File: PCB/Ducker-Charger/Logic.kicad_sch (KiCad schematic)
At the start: 47 parts, among them CN1 C_Pack04, IC2 TPS54202HDDCT, J6 Debug, J7 Conn_01x08, J8 Conn_01x07, SW1 EC11E15244G1, U7 STM32F401RBT6, Y1 16MHz

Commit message: fix: minor fixes
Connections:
- net BOOT is gone; now on net BOOT0: U7.60 (BOOT0)
- net SCL is gone; now on net I2C_LP.SCL: J7.4 (Pin_4)
- net SDA is gone; now on net I2C_LP.SDA: J7.3 (Pin_3)
- net ENC_A: no longer C52.1, R50.2, SW1.B, U7.38 (PC7)
- new net ENC_B: C52.1, R50.2, SW1.B, U7.38 (PC7)
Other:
- moved on the sheet: CN1, D21, JP1, R31, R32, R34, R52, R53, R54, RN1, U7

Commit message: feat: updated footprints
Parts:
- C28, C31, C32, C33, C34, C35, C38, C39: footprint (none) -> Capacitor_SMD:C_0805_2012Metric
- C29, C30, C36, C37, C40, C51, C52, C53: footprint (none) -> Capacitor_SMD:C_0603_1608Metric
- CN1: footprint (none) -> Resistor_SMD:R_Array_Concave_4x0603
- CVBAT1, R26, R27, R28, R29, R30, R31, R32, R49, R50, R51, R52, R53: footprint (none) -> Resistor_SMD:R_0603_1608Metric
- FB1: footprint (none) -> Inductor_SMD:L_0603_1608Metric
- L5: footprint (none) -> Inductor_SMD:L_6.3x6.3_H3
- RN1: footprint (none) -> Resistor_SMD:R_Array_Convex_4x0603
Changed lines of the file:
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@@
 			)
 		)
-		(property "Footprint" ""
+		(property "Footprint" "Capacitor_SMD:C_0805_2012Metric"
 			(at 100.0252 35.56 0)
 			(effects
@@
 			)
 		)
-		(property "Footprint" ""
+		(property "Footprint" "Capacitor_SMD:C_0805_2012Metric"
 			(at 88.5952 35.56 0)
 			(effects
@@
 			)
 		)
-		(property "Footprint" ""
+		(property "Footprint" "Capacitor_SMD:C_0603_1608Metric"
 			(at 45.4152 34.29 0)
 			(effects
@@
 			)
 		)
-		(property "Footprint" ""
+		(property "Footprint" "Capacitor_SMD:C_0603_1608Metric"
 			(at 60.6552 160.02 0)
 			(effects
@@
 			)
 		)
-		(property "Footprint" ""
+		(property "Footprint" "Resistor_SMD:R_0603_1608Metric"
 			(at 176.022 82.55 90)
 			(effects
@@
 			)
 		)
-		(property "Footprint" ""
+		(property "Footprint" "Resistor_SMD:R_0603_1608Metric"
 			(at 176.022 127 90)
 			(effects
@@
 			)
 		)
-		(property "Footprint" ""
+		(property "Footprint" "Resistor_SMD:R_Array_Convex_4x0603"
 			(at 253.365 86.36 90)
 			(effects
@@
 			)
 		)
-		(property "Footprint" ""
+		(property "Footprint" "Resistor_SMD:R_Array_Concave_4x0603"
 			(at 253.365 109.22 90)
 			(effects
@@
 			)
 		)
-		(property "Footprint" ""
+		(property "Footprint" "Resistor_SMD:R_0603_1608Metric"
 			(at 57.912 138.43 90)
 			(effects
@@
 			)
 		)
-		(property "Footprint" ""
+		(property "Footprint" "Capacitor_SMD:C_0603_1608Metric"
 			(at 68.2752 160.02 0)
 			(effects
@@
 			)
 		)
-		(property "Footprint" ""
+		(property "Footprint" "Resistor_SMD:R_0603_1608Metric"
 			(at 193.802 46.99 90)
 			(effects
@@
 			)
 		)
-		(property "Footprint" ""
+		(property "Footprint" "Resistor_SMD:R_0603_1608Metric"
 			(at 106.172 34.29 90)
 			(effects
@@
 			)
 		)
-		(property "Footprint" ""
+		(property "Footprint" "Capacitor_SMD:C_0805_2012Metric"
 			(at 171.1452 41.91 0)
 			(effects
@@
 			)
 		)
-		(property "Footprint" ""
+		(property "Footprint" "Capacitor_SMD:C_0805_2012Metric"
 			(at 185.7248 43.18 0)
 			(effects
@@
 			)
 		)
-		(property "Footprint" ""
+		(property "Footprint" "Capacitor_SMD:C_0603_1608Metric"
 			(at 32.7152 152.4 0)
 			(effects
@@
 			)
 		)
-		(property "Footprint" ""
+		(property "Footprint" "Capacitor_SMD:C_0805_2012Metric"
 			(at 25.0952 113.03 0)
 			(effects
@@
 			)
 		)
-		(property "Footprint" ""
+		(property "Footprint" "Resistor_SMD:R_0603_1608Metric"
 			(at 106.172 44.45 90)
 			(effects
@@
 			)
 		)
-		(property "Footprint" ""
+		(property "Footprint" "Resistor_SMD:R_0603_1608Metric"
 			(at 65.532 138.43 90)
 			(effects
@@
 			)
 		)
-		(property "Footprint" ""
+		(property "Footprint" "Resistor_SMD:R_0603_1608Metric"
 			(at 167.132 85.09 90)
 			(effects
@@
 			)
 		)
-		(property "Footprint" ""
+		(property "Footprint" "Resistor_SMD:R_0603_1608Metric"
 			(at 193.802 55.88 90)
 			(effects
@@
 			)
 		)
-		(property "Footprint" ""
+		(property "Footprint" "Capacitor_SMD:C_0603_1608Metric"
 			(at 25.0952 55.88 0)
 			(effects
@@
 			)
 		)
-		(property "Footprint" ""
+		(property "Footprint" "Capacitor_SMD:C_0805_2012Metric"
 			(at 45.4152 78.74 0)
 			(effects
@@
 			)
 		)
-		(property "Footprint" ""
+		(property "Footprint" "Resistor_SMD:R_0603_1608Metric"
 			(at 29.972 140.97 90)
 			(effects
@@
 			)
 		)
-		(property "Footprint" ""
+		(property "Footprint" "Capacitor_SMD:C_0603_1608Metric"
 			(at 45.4152 55.88 0)
 			(effects
@@
 			)
 		)
-		(property "Footprint" ""
+		(property "Footprint" "Capacitor_SMD:C_0603_1608Metric"
 			(at 25.0952 34.29 0)
 			(effects
@@
 			)
 		)
-		(property "Footprint" ""
+		(property "Footprint" "Inductor_SMD:L_0603_1608Metric"
 			(at 22.352 100.33 90)
 			(effects
@@
 			)
 		)
-		(property "Footprint" ""
+		(property "Footprint" "Resistor_SMD:R_0603_1608Metric"
 			(at 167.132 129.54 90)
 			(effects
@@
 			)
 		)
-		(property "Footprint" ""
+		(property "Footprint" "Resistor_SMD:R_0603_1608Metric"
 			(at 193.802 38.1 90)
 			(effects
@@
 			)
 		)
-		(property "Footprint" ""
+		(property "Footprint" "Capacitor_SMD:C_0805_2012Metric"
 			(at 154.94 26.9748 0)
 			(effects
@@
 			)
 		)
-		(property "Footprint" ""
+		(property "Footprint" "Capacitor_SMD:C_0603_1608Metric"
 			(at 35.2552 113.03 0)
 			(effects
@@
 			)
 		)
-		(property "Footprint" ""
+		(property "Footprint" "Inductor_SMD:L_6.3x6.3_H3"
 			(at 162.56 34.29 0)
 			(effects
@@
 			)
 		)
-		(property "Footprint" ""
+		(property "Footprint" "Resistor_SMD:R_0603_1608Metric"
 			(at 25.0952 78.74 0)
 			(effects
@@
 			)
 		)
-		(property "Footprint" ""
+		(property "Footprint" "Capacitor_SMD:C_0805_2012Metric"
 			(at 181.3052 41.91 0)
 			(effects

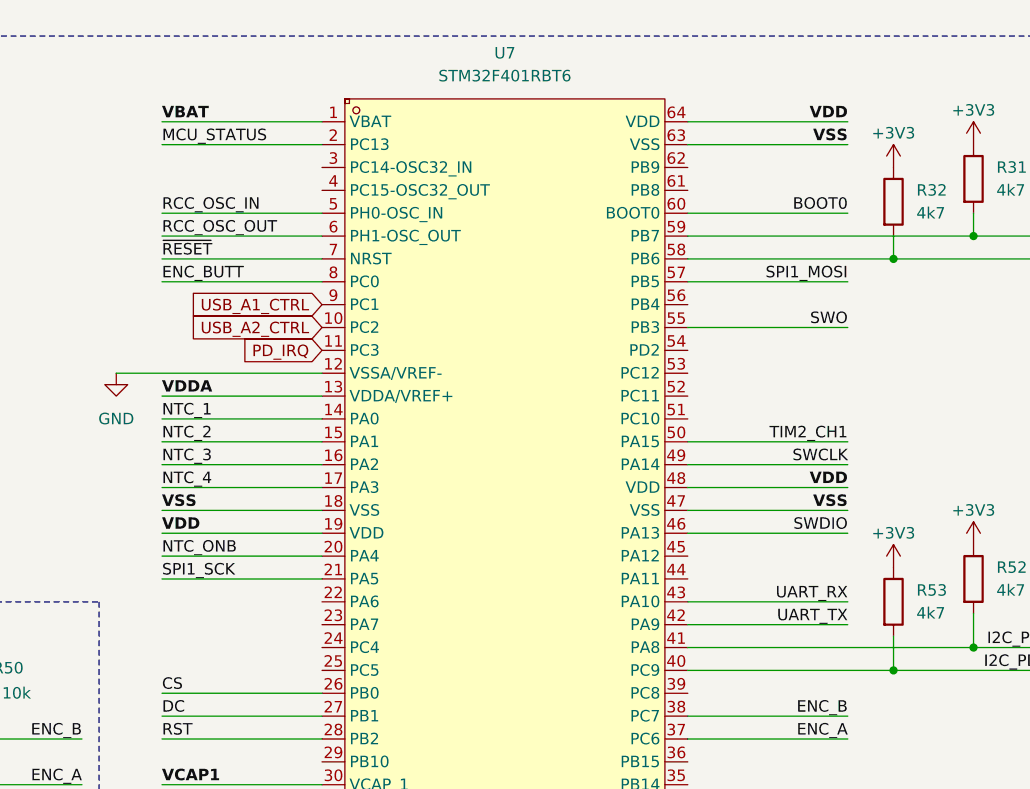
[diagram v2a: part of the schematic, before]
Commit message: fix: updated config based on CubeMX
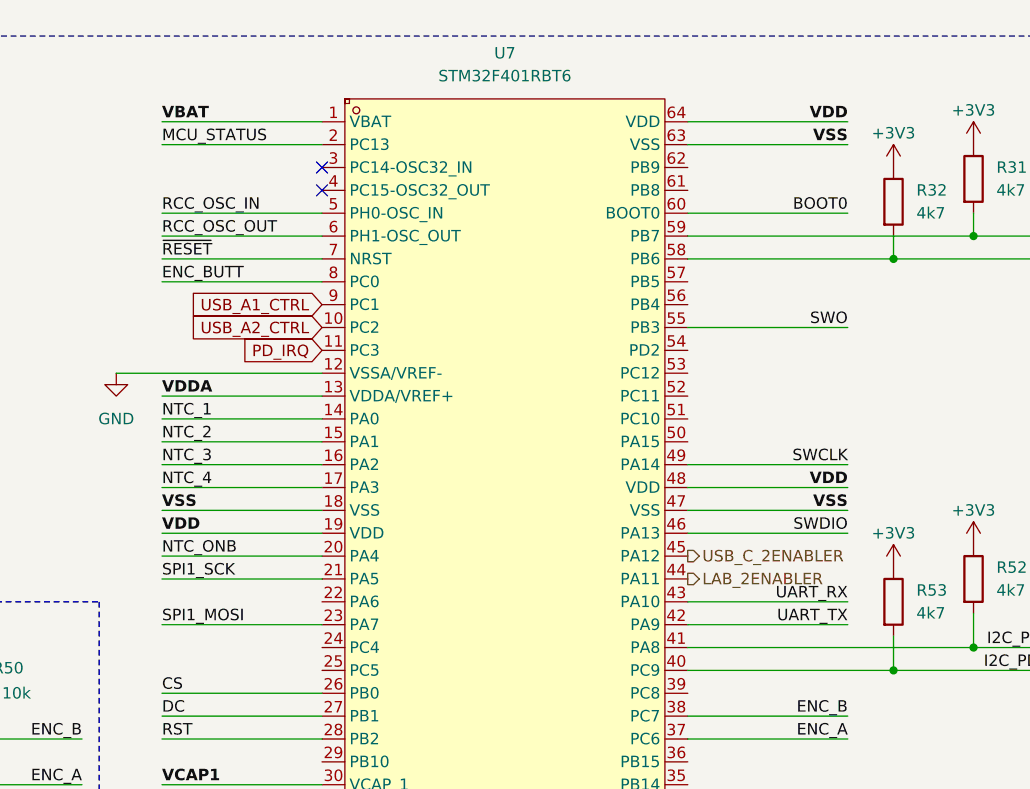
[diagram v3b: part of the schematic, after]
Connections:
- net SPI1_MOSI: now also U7.23 (PA7); no longer U7.57 (PB5)
- net LAB_2ENABLER: now reaches U7.44 (PA11)
- net USB_C_2ENABLER: now reaches U7.45 (PA12)
- net TIM2_CH1: no longer names the net of U7.50 (PA15)
- no-connect marks 2 -> 4
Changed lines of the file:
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@@
+	)
+	(no_connect
+		(at 105.41 83.82)
 	)
 	(no_connect
 		(at 262.89 44.45)
+	)
+	(no_connect
+		(at 105.41 81.28)
 	)
 	(bus_entry
@@
 	(wire
 		(pts
+			(xy 105.41 132.08) (xy 87.63 132.08)
+		)
+		(stroke
+			(width 0)
+			(type default)
+		)
+	)
+	(wire
+		(pts
 			(xy 257.81 92.71) (xy 270.51 92.71)
 		)
@@
 	(wire
 		(pts
-			(xy 146.05 93.98) (xy 163.83 93.98)
-		)
-		(stroke
-			(width 0)
-			(type default)
-		)
-	)
-	(wire
-		(pts
 			(xy 215.9 154.94) (xy 229.87 154.94)
 		)
@@
 		(pts
 			(xy 24.13 104.14) (xy 24.13 105.41)
-		)
-		(stroke
-			(width 0)
-			(type default)
-		)
-	)
-	(wire
-		(pts
-			(xy 146.05 111.76) (xy 163.83 111.76)
 		)
 		(stroke
@@
 		)
 	)
-	(label "TIM2_CH1"
-		(at 163.83 111.76 180)
-		(effects
-			(font
-				(size 1.27 1.27)
-				(thickness 0.1588)
-			)
-			(justify right bottom)
-		)
-	)
 	(label "I2C_PD.SDA"
 		(at 229.87 148.59 180)
@@
 		)
 	)
+	(label "SPI1_MOSI"
+		(at 87.63 132.08 0)
+		(effects
+			(font
+				(size 1.27 1.27)
+				(thickness 0.1588)
+			)
+			(justify left bottom)
+		)
+	)
 	(label "NTC_2"
 		(at 233.68 97.79 0)
@@
 			(font
 				(size 1.27 1.27)
-			)
-			(justify right bottom)
-		)
-	)
-	(label "SPI1_MOSI"
-		(at 163.83 93.98 180)
-		(effects
-			(font
-				(size 1.27 1.27)
-				(thickness 0.1588)
 			)
 			(justify right bottom)
@@
 		)
 	)
+	(hierarchical_label "LAB_2ENABLER"
+		(shape output)
+		(at 146.05 127 0)
+		(effects
+			(font
+				(size 1.27 1.27)
+			)
+			(justify left)
+		)
+	)
+	(hierarchical_label "USB_C_2ENABLER"
+		(shape output)
+		(at 146.05 124.46 0)
+		(effects
+			(font
+				(size 1.27 1.27)
+			)
+			(justify left)
+		)
+	)

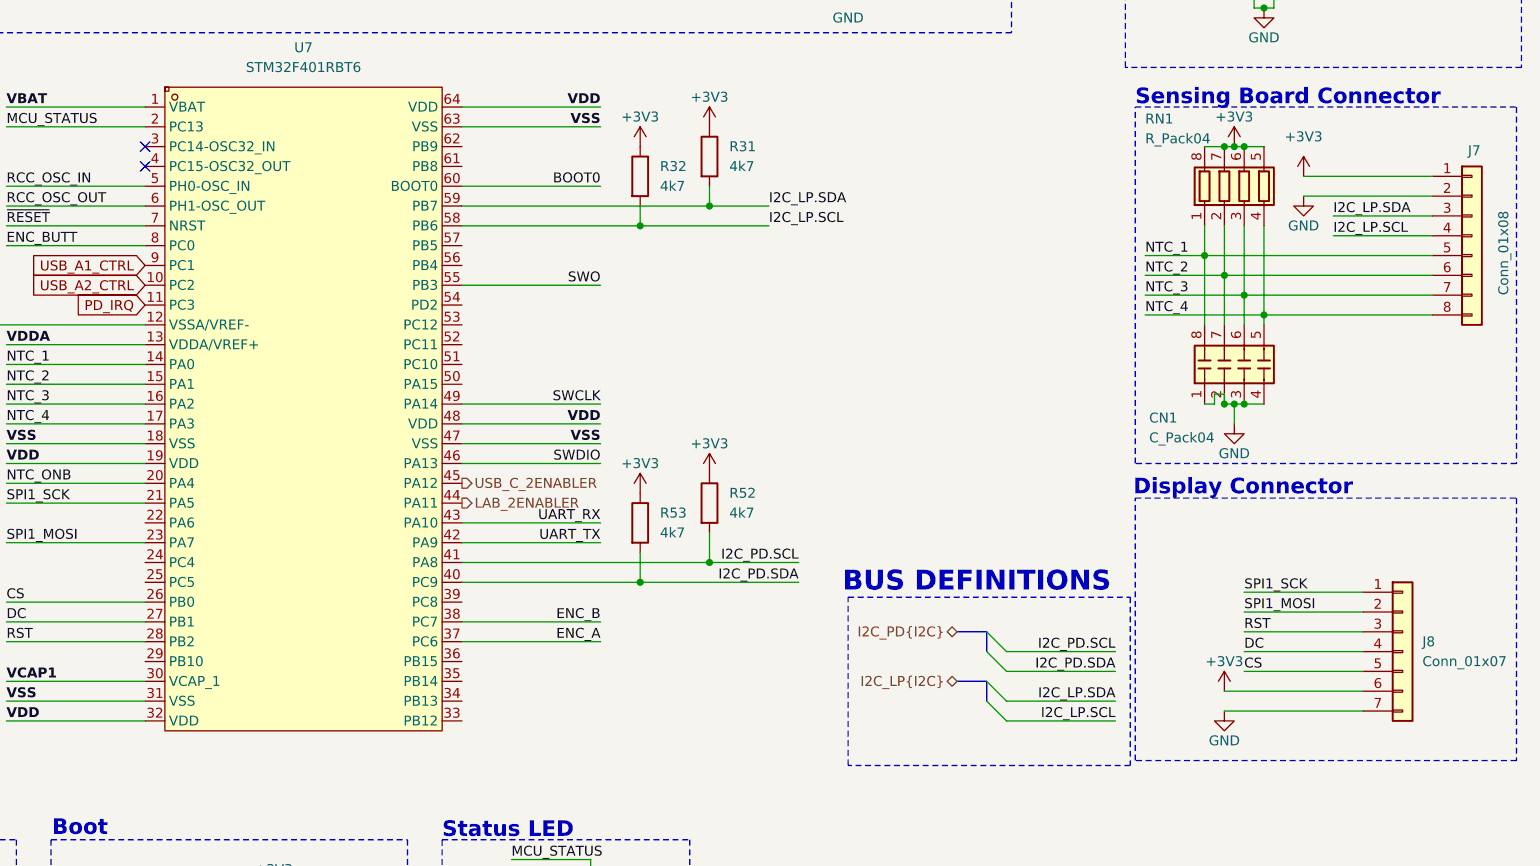
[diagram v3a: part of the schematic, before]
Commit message: fix: added missing connections
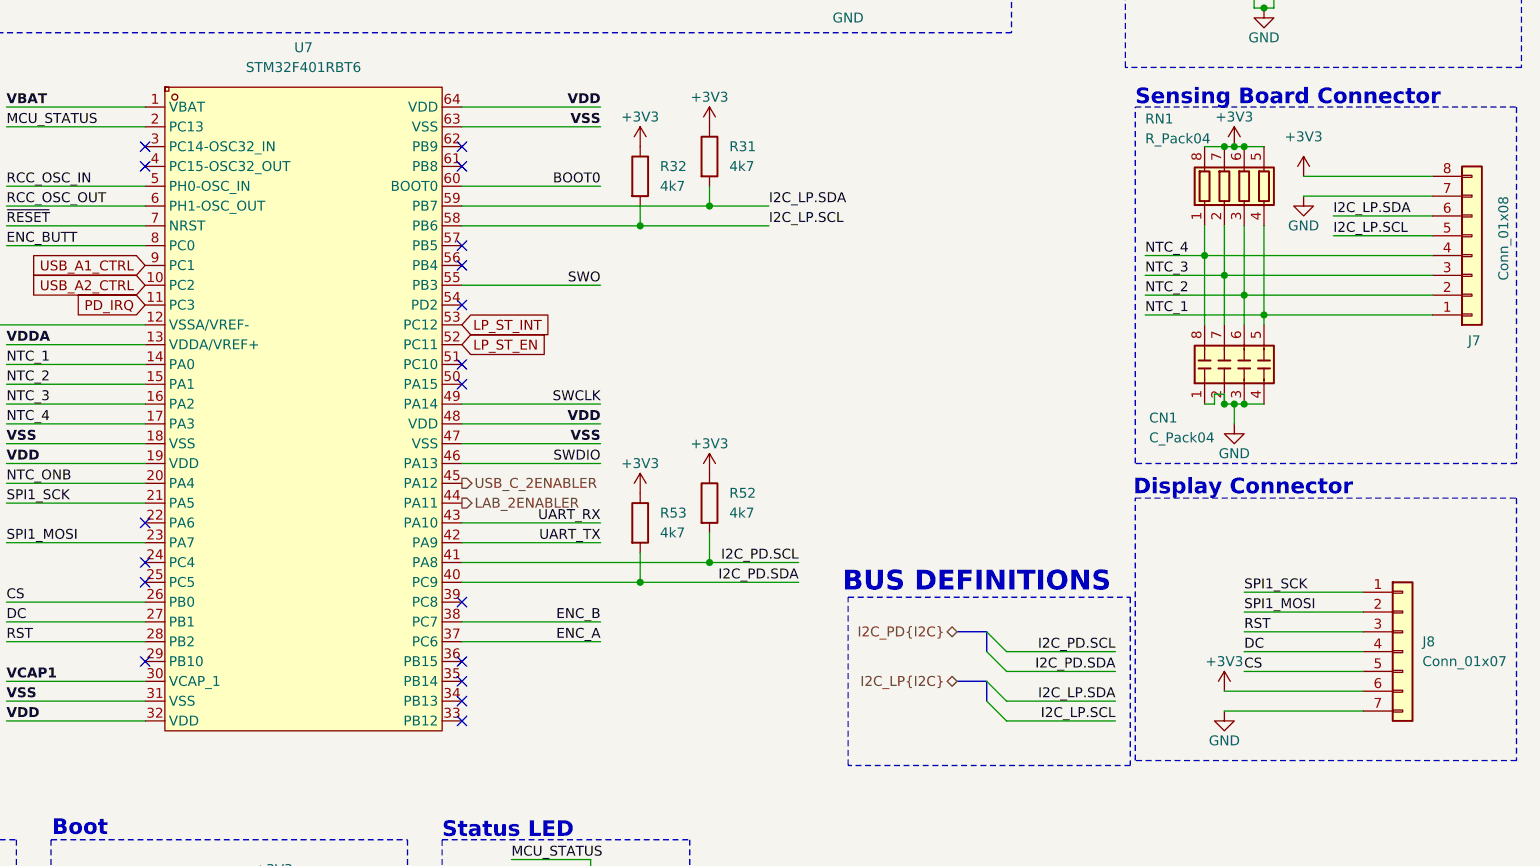
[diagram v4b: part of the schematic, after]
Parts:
- J7: footprint (none) -> Connector_FFC-FPC:Molex_200528-0080_1x08-1MP_P1.00mm_Horizontal
- J8: footprint (none) -> Connector_JST:JST_XH_S7B-XH-A_1x07_P2.50mm_Horizontal
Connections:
- net +3V3: now also J7.8 (Pin_8); no longer J7.1 (Pin_1)
- net GND: now also J7.7 (Pin_7); no longer J7.2 (Pin_2)
- net I2C_LP.SCL: now also J7.5 (Pin_5); no longer J7.4 (Pin_4)
- net I2C_LP.SDA: now also J7.6 (Pin_6); no longer J7.3 (Pin_3)
- net NTC_1: now also CN1.5 (R4.2), J7.1 (Pin_1), RN1.4 (R4.1); no longer CN1.8 (R1.2), J7.5 (Pin_5), RN1.1 (R1.1)
- net NTC_2: now also CN1.6 (R3.2), J7.2 (Pin_2), RN1.3 (R3.1); no longer CN1.7 (R2.2), J7.6 (Pin_6), RN1.2 (R2.1)
- net NTC_3: now also CN1.7 (R2.2), J7.3 (Pin_3), RN1.2 (R2.1); no longer CN1.6 (R3.2), J7.7 (Pin_7), RN1.3 (R3.1)
- net NTC_4: now also CN1.8 (R1.2), J7.4 (Pin_4), RN1.1 (R1.1); no longer CN1.5 (R4.2), J7.8 (Pin_8), RN1.4 (R4.1)
- net LP_ST_EN: now reaches U7.52 (PC11)
- net LP_ST_INT: now reaches U7.53 (PC12)
- no-connect marks 4 -> 20
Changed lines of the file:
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@@
 	)
 	(no_connect
+		(at 146.05 83.82)
+	)
+	(no_connect
+		(at 146.05 109.22)
+	)
+	(no_connect
+		(at 105.41 134.62)
+	)
+	(no_connect
+		(at 146.05 93.98)
+	)
+	(no_connect
+		(at 146.05 154.94)
+	)
+	(no_connect
 		(at 262.89 49.53)
 	)
 	(no_connect
+		(at 146.05 81.28)
+	)
+	(no_connect
 		(at 105.41 83.82)
 	)
 	(no_connect
+		(at 146.05 149.86)
+	)
+	(no_connect
+		(at 105.41 147.32)
+	)
+	(no_connect
+		(at 105.41 129.54)
+	)
+	(no_connect
+		(at 146.05 101.6)
+	)
+	(no_connect
+		(at 146.05 96.52)
+	)
+	(no_connect
+		(at 146.05 147.32)
+	)
+	(no_connect
+		(at 146.05 139.7)
+	)
+	(no_connect
+		(at 105.41 137.16)
+	)
+	(no_connect
+		(at 146.05 111.76)
+	)
+	(no_connect
+		(at 146.05 152.4)
+	)
+	(no_connect
 		(at 262.89 44.45)
 	)
@@
 		)
 	)
-	(label "NTC_4"
-		(at 233.68 102.87 0)
+	(label "VDD"
+		(at 87.63 154.94 0)
 		(effects
 			(font
 				(size 1.27 1.27)
+				(thickness 0.254)
+				(bold yes)
 			)
 			(justify left bottom)
 		)
 	)
-	(label "VDD"
-		(at 87.63 154.94 0)
+	(label "NTC_1"
+		(at 233.68 102.87 0)
 		(effects
 			(font
 				(size 1.27 1.27)
-				(thickness 0.254)
-				(bold yes)
 			)
 			(justify left bottom)
@@
 		)
 	)
+	(label "NTC_4"
+		(at 233.68 95.25 0)
+		(effects
+			(font
+				(size 1.27 1.27)
+			)
+			(justify left bottom)
+		)
+	)
 	(label "VSS"
 		(at 87.63 119.38 0)
@@
 		)
 	)
-	(label "NTC_3"
-		(at 233.68 100.33 0)
-		(effects
-			(font
-				(size 1.27 1.27)
-			)
-			(justify left bottom)
-		)
-	)
 	(label "SWCLK"
 		(at 275.59 36.83 180)
@@
 		)
 	)
-	(label "NTC_2"
-		(at 233.68 97.79 0)
-		(effects
-			(font
-				(size 1.27 1.27)
-			)
-			(justify left bottom)
-		)
-	)
-	(label "NTC_1"
-		(at 233.68 95.25 0)
-		(effects
-			(font
-				(size 1.27 1.27)
-			)
-			(justify left bottom)
-		)
-	)
 	(label "UART_RX"
 		(at 275.59 54.61 180)
@@
 		)
 	)
+	(label "NTC_2"
+		(at 233.68 100.33 0)
+		(effects
+			(font
+				(size 1.27 1.27)
+			)
+			(justify left bottom)
+		)
+	)
 	(label "NTC_ONB"
 		(at 87.63 124.46 0)
@@
 		)
 	)
+	(label "NTC_3"
+		(at 233.68 97.79 0)
+		(effects
+			(font
+				(size 1.27 1.27)
+			)
+			(justify left bottom)
+		)
+	)
 	(label "VDD"
 		(at 163.83 76.2 180)
@@
 		)
 	)
+	(global_label "LP_ST_EN"
+		(shape input)
+		(at 146.05 106.68 0)
+		(fields_autoplaced yes)
+		(effects
+			(font
+				(size 1.27 1.27)
+			)
+			(justify left)
+		)
+		(property "Intersheetrefs" "${INTERSHEET_REFS}"
+			(at 158.3485 106.68 0)
+			(effects
+				(font
+					(size 1.27 1.27)
+				)
+				(justify left)
+				(hide yes)
+			)
+		)
+	)
 	(global_label "PD_IRQ"
 		(shape input)
@@
 		)
 	)
+	(global_label "LP_ST_INT"
+		(shape input)
+		(at 146.05 104.14 0)
+		(fields_autoplaced yes)
+		(effects
+			(font
+				(size 1.27 1.27)
+			)
+			(justify left)
+		)
+		(property "Intersheetrefs" "${INTERSHEET_REFS}"
+			(at 157.9251 104.14 0)
+			(effects
+				(font
+					(size 1.27 1.27)
+				)
+				(justify left)
+				(hide yes)
+			)
+		)
+	)
 	(global_label "USB_A2_CTRL"
 		(shape input)
@@
 			)
 		)
-		(property "Footprint" ""
+		(property "Footprint" "Connector_JST:JST_XH_S7B-XH-A_1x07_P2.50mm_Horizontal"
 			(at 266.7 146.05 0)
 			(effects
@@
 	(symbol
 		(lib_id "Connector_Generic:Conn_01x08")
-		(at 275.59 92.71 0)
+		(at 275.59 95.25 0)
+		(mirror x)
 		(unit 1)
 		(exclude_from_sim no)
@@
 		(dnp no)
 		(property "Reference" "J7"
-			(at 275.082 81.788 0)
+			(at 275.082 106.172 0)
 			(effects
 				(font
@@
 		)
 		(property "Value" "Conn_01x08"
-			(at 279.654 100.33 90)
+			(at 279.654 87.63 90)
 			(effects
 				(font
@@
 			)
 		)
-		(property "Footprint" ""
-			(at 275.59 92.71 0)
+		(property "Footprint" "Connector_FFC-FPC:Molex_200528-0080_1x08-1MP_P1.00mm_Horizontal"
+			(at 275.59 95.25 0)
 			(effects
 				(font
@@
 		)
 		(property "Datasheet" "~"
-			(at 275.59 92.71 0)
+			(at 275.59 95.25 0)
 			(effects
 				(font
@@
 		)
 		(property "Description" "Generic connector, single row, 01x08, script generated (kicad-library-utils/schlib/autogen/connector/)"
-			(at 275.59 92.71 0)
+			(at 275.59 95.25 0)
 			(effects
 				(font
@@
 		)
 		(instances
-			(project ""
+			(project "Ducker-Charger"
 				(path "/74790d6c-a68e-4e6d-b4a9-43de1843f817/b1375a06-d47d-478c-835c-6ba88db99bcf"
 					(reference "J7")

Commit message: fix: missing files
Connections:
- net +BATT: no longer C31.1, C32.1, IC2.3 (VIN), R26.1
- net SPI1_MOSI: now also U7.57 (PB5); no longer U7.23 (PA7)
- net HP.IADPT: now reaches U7.22 (PA6)
- net HP.PSYS: now reaches U7.24 (PC4)
- net HP.CHRG_OK: now reaches U7.34 (PB13)
- net HP.PD_IRQ: now reaches U7.35 (PB14)
- net HP.EN_OTG: now reaches U7.36 (PB15)
- new net HP.IBAT: U7.23 (PA7)
- new net VSYS: C31.1, C32.1, IC2.3 (VIN), R26.1
- no-connect marks 20 -> 14
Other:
- note added: "Powering the regulator via VSYS ensures immediate MCU boot from VBUS (USB-C HP), even with a depleted or missing battery"
